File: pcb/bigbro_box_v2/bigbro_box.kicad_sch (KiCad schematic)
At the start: 45 parts, among them J1 CT_AMP, J2 Display, J3 Mains, J4 UART flashing, J5 Conn_01x02, J6 Relay, K1 G5LE-1, Q1 MMBT3904, Q2 MMBT3904, Q3 BSS138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

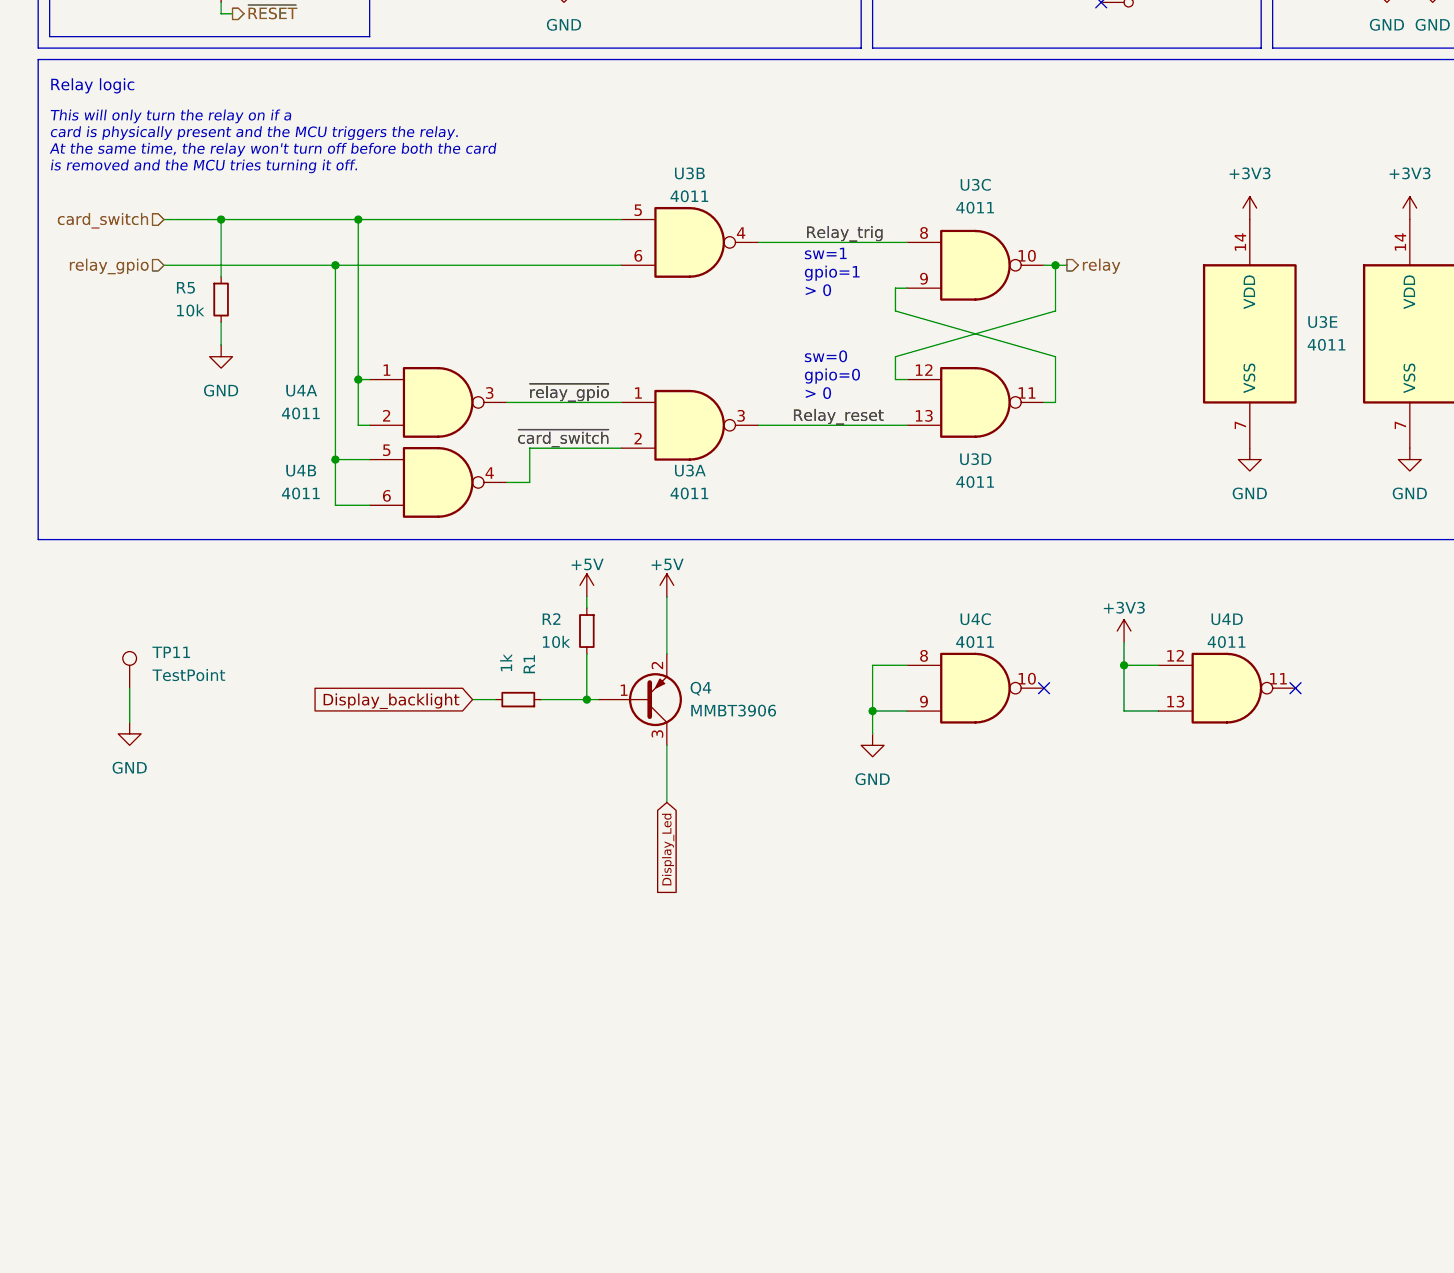
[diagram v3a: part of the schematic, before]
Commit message: New fuse holder, rearrange footprints.
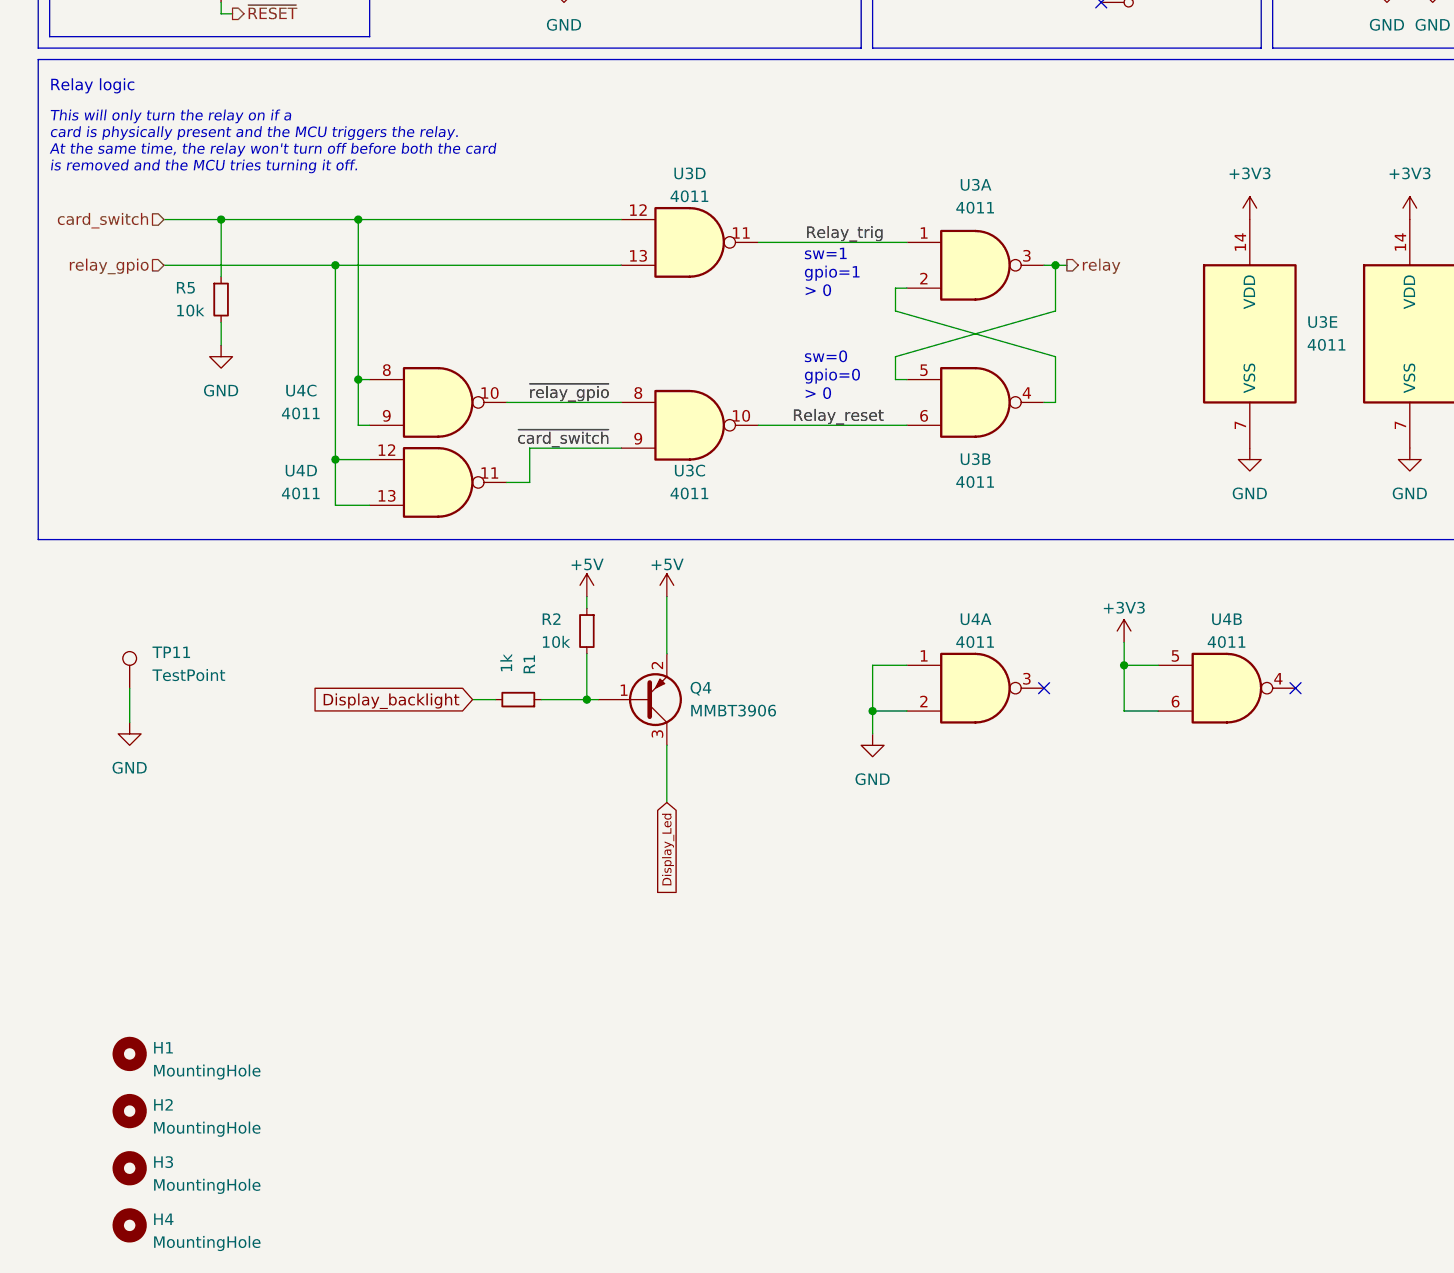
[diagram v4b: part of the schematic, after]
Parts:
- added H1, H2, H3, H4: MountingHole, MountingHole:MountingHole_3.2mm_M3, symbol Mechanical:MountingHole
- F1: footprint Fuse:Fuseholder_Littelfuse_445_030_series_5x20mm -> modules:Fuseholder5x20_horiz_SemiClosed_Casing10x25mm
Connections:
- net +3V3: now also U4.5, U4.6; no longer U4.12, U4.13
- net GND: now also U4.1, U4.2; no longer U4.8, U4.9
- net Relay_reset: now also U3.10, U3.6; no longer U3.13, U3.3
- net Relay_trig: now also U3.1, U3.11; no longer U3.4, U3.8
- net card_switch: now also U3.12, U4.8, U4.9; no longer U3.5, U4.1, U4.2
- net relay: now also U3.3, U3.5; no longer U3.10, U3.12
- net relay_gpio: now also U3.13, U4.12, U4.13; no longer U3.6, U4.5, U4.6
- net ~{card_switch}: now also U3.9, U4.11; no longer U3.2, U4.4
- net ~{relay_gpio}: now also U3.8, U4.10; no longer U3.1, U4.3
- new net: U3.2, U3.4
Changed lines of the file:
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@@
     )
   )
-  (symbol (lib_id "4xxx:4011") (at 119.38 142.24 0) (unit 4)
+  (symbol (lib_id "4xxx:4011") (at 119.38 142.24 0) (unit 2)
     (in_bom yes) (on_board yes) (dnp no)
     (property "Reference" "U3" (at 119.38 148.59 0)
@@
       (project "bigbro_box"
         (path "/212a0d71-cc7b-49f8-b4ca-a935e5355dca"
-          (reference "U3") (unit 4)
+          (reference "U3") (unit 2)
         )
       )
@@
     )
   )
+  (symbol (lib_id "Mechanical:MountingHole") (at 25.4 220.98 0) (unit 1)
+    (in_bom yes) (on_board yes) (dnp no) (fields_autoplaced)
+    (property "Reference" "H2" (at 27.94 220.345 0)
+      (effects (font (size 1.27 1.27)) (justify left))
+    )
+    (property "Value" "MountingHole" (at 27.94 222.885 0)
+      (effects (font (size 1.27 1.27)) (justify left))
+    )
+    (property "Footprint" "MountingHole:MountingHole_3.2mm_M3" (at 25.4 220.98 0)
+      (effects (font (size 1.27 1.27)) hide)
+    )
+    (property "Datasheet" "~" (at 25.4 220.98 0)
+      (effects (font (size 1.27 1.27)) hide)
+    )
+    (instances
+      (project "bigbro_box"
+        (path "/212a0d71-cc7b-49f8-b4ca-a935e5355dca"
+          (reference "H2") (unit 1)
+        )
+      )
+    )
+  )
   (symbol (lib_id "Connector:TestPoint") (at 91.44 49.53 270) (unit 1)
     (in_bom yes) (on_board yes) (dnp no)
@@
     )
   )
+  (symbol (lib_id "Mechanical:MountingHole") (at 25.4 227.33 0) (unit 1)
+    (in_bom yes) (on_board yes) (dnp no) (fields_autoplaced)
+    (property "Reference" "H3" (at 27.94 226.695 0)
+      (effects (font (size 1.27 1.27)) (justify left))
+    )
+    (property "Value" "MountingHole" (at 27.94 229.235 0)
+      (effects (font (size 1.27 1.27)) (justify left))
+    )
+    (property "Footprint" "MountingHole:MountingHole_3.2mm_M3" (at 25.4 227.33 0)
+      (effects (font (size 1.27 1.27)) hide)
+    )
+    (property "Datasheet" "~" (at 25.4 227.33 0)
+      (effects (font (size 1.27 1.27)) hide)
+    )
+    (instances
+      (project "bigbro_box"
+        (path "/212a0d71-cc7b-49f8-b4ca-a935e5355dca"
+          (reference "H3") (unit 1)
+        )
+      )
+    )
+  )
   (symbol (lib_id "power:GND") (at 341.63 111.76 0) (unit 1)
     (in_bom yes) (on_board yes) (dnp no)
@@
     )
   )
-  (symbol (lib_id "4xxx:4011") (at 147.32 173.99 0) (unit 4)
+  (symbol (lib_id "4xxx:4011") (at 147.32 173.99 0) (unit 2)
     (in_bom yes) (on_board yes) (dnp no) (fields_autoplaced)
     (property "Reference" "U4" (at 147.3117 166.37 0)
@@
       (project "bigbro_box"
         (path "/212a0d71-cc7b-49f8-b4ca-a935e5355dca"
-          (reference "U4") (unit 4)
+          (reference "U4") (unit 2)
         )
       )
@@
       (effects (font (size 1.27 1.27)))
     )
-    (property "Footprint" "Fuse:Fuseholder_Littelfuse_445_030_series_5x20mm" (at 330.2 39.37 0)
+    (property "Footprint" "modules:Fuseholder5x20_horiz_SemiClosed_Casing10x25mm" (at 330.2 39.37 0)
       (effects (font (size 1.27 1.27)) hide)
     )
@@
     )
   )
-  (symbol (lib_id "4xxx:4011") (at 59.69 142.24 0) (unit 1)
+  (symbol (lib_id "4xxx:4011") (at 59.69 142.24 0) (unit 3)
     (in_bom yes) (on_board yes) (dnp no)
     (property "Reference" "U4" (at 44.45 140.97 0)
@@
       (project "bigbro_box"
         (path "/212a0d71-cc7b-49f8-b4ca-a935e5355dca"
-          (reference "U4") (unit 1)
+          (reference "U4") (unit 3)
         )
       )
@@
     )
   )
-  (symbol (lib_id "4xxx:4011") (at 119.38 173.99 0) (unit 3)
+  (symbol (lib_id "4xxx:4011") (at 119.38 173.99 0) (unit 1)
     (in_bom yes) (on_board yes) (dnp no) (fields_autoplaced)
     (property "Reference" "U4" (at 119.3717 166.37 0)
@@
       (project "bigbro_box"
         (path "/212a0d71-cc7b-49f8-b4ca-a935e5355dca"
-          (reference "U4") (unit 3)
+          (reference "U4") (unit 1)
         )
       )
@@
     )
   )
-  (symbol (lib_id "4xxx:4011") (at 59.69 151.13 0) (unit 2)
+  (symbol (lib_id "4xxx:4011") (at 59.69 151.13 0) (unit 4)
     (in_bom yes) (on_board yes) (dnp no)
     (property "Reference" "U4" (at 44.45 149.86 0)
@@
       (project "bigbro_box"
         (path "/212a0d71-cc7b-49f8-b4ca-a935e5355dca"
-          (reference "U4") (unit 2)
-        )
-      )
-    )
-  )
-  (symbol (lib_id "4xxx:4011") (at 87.63 144.78 0) (unit 1)
+          (reference "U4") (unit 4)
+        )
+      )
+    )
+  )
+  (symbol (lib_id "4xxx:4011") (at 87.63 144.78 0) (unit 3)
     (in_bom yes) (on_board yes) (dnp no)
     (property "Reference" "U3" (at 87.63 149.86 0)
@@
       (project "bigbro_box"
         (path "/212a0d71-cc7b-49f8-b4ca-a935e5355dca"
-          (reference "U3") (unit 1)
+          (reference "U3") (unit 3)
         )
       )
@@
     )
   )
+  (symbol (lib_id "Mechanical:MountingHole") (at 25.4 233.68 0) (unit 1)
+    (in_bom yes) (on_board yes) (dnp no) (fields_autoplaced)
+    (property "Reference" "H4" (at 27.94 233.045 0)
+      (effects (font (size 1.27 1.27)) (justify left))
+    )
+    (property "Value" "MountingHole" (at 27.94 235.585 0)
+      (effects (font (size 1.27 1.27)) (justify left))
+    )
+    (property "Footprint" "MountingHole:MountingHole_3.2mm_M3" (at 25.4 233.68 0)
+      (effects (font (size 1.27 1.27)) hide)
+    )
+    (property "Datasheet" "~" (at 25.4 233.68 0)
+      (effects (font (size 1.27 1.27)) hide)
+    )
+    (instances
+      (project "bigbro_box"
+        (path "/212a0d71-cc7b-49f8-b4ca-a935e5355dca"
+          (reference "H4") (unit 1)
+        )
+      )
+    )
+  )
   (symbol (lib_id "power:+3V3") (at 387.35 38.1 0) (unit 1)
     (in_bom yes) (on_board yes) (dnp no)
@@
     )
   )
-  (symbol (lib_id "4xxx:4011") (at 87.63 124.46 0) (unit 2)
+  (symbol (lib_id "4xxx:4011") (at 87.63 124.46 0) (unit 4)
     (in_bom yes) (on_board yes) (dnp no)
     (property "Reference" "U3" (at 87.63 116.84 0)
@@
       (project "bigbro_box"
         (path "/212a0d71-cc7b-49f8-b4ca-a935e5355dca"
-          (reference "U3") (unit 2)
+          (reference "U3") (unit 4)
+        )
+      )
+    )
+  )
+  (symbol (lib_id "Mechanical:MountingHole") (at 25.4 214.63 0) (unit 1)
+    (in_bom yes) (on_board yes) (dnp no) (fields_autoplaced)
+    (property "Reference" "H1" (at 27.94 213.995 0)
+      (effects (font (size 1.27 1.27)) (justify left))
+    )
+    (property "Value" "MountingHole" (at 27.94 216.535 0)
+      (effects (font (size 1.27 1.27)) (justify left))
+    )
+    (property "Footprint" "MountingHole:MountingHole_3.2mm_M3" (at 25.4 214.63 0)
+      (effects (font (size 1.27 1.27)) hide)
+    )
+    (property "Datasheet" "~" (at 25.4 214.63 0)
+      (effects (font (size 1.27 1.27)) hide)
+    )
+    (instances
+      (project "bigbro_box"
+        (path "/212a0d71-cc7b-49f8-b4ca-a935e5355dca"
+          (reference "H1") (unit 1)
         )
       )
@@
     )
   )
-  (symbol (lib_id "4xxx:4011") (at 119.38 127 0) (unit 3)
+  (symbol (lib_id "4xxx:4011") (at 119.38 127 0) (unit 1)
     (in_bom yes) (on_board yes) (dnp no) (fields_autoplaced)
     (property "Reference" "U3" (at 119.38 118.11 0)
@@
       (project "bigbro_box"
         (path "/212a0d71-cc7b-49f8-b4ca-a935e5355dca"
-          (reference "U3") (unit 3)
-        )
-      )
+          (reference "U3") (unit 1)
+        )
+      )
